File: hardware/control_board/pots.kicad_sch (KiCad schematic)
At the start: 38 parts, among them IC4 4051, IC5 4051, IC6 4051, IC7 4051

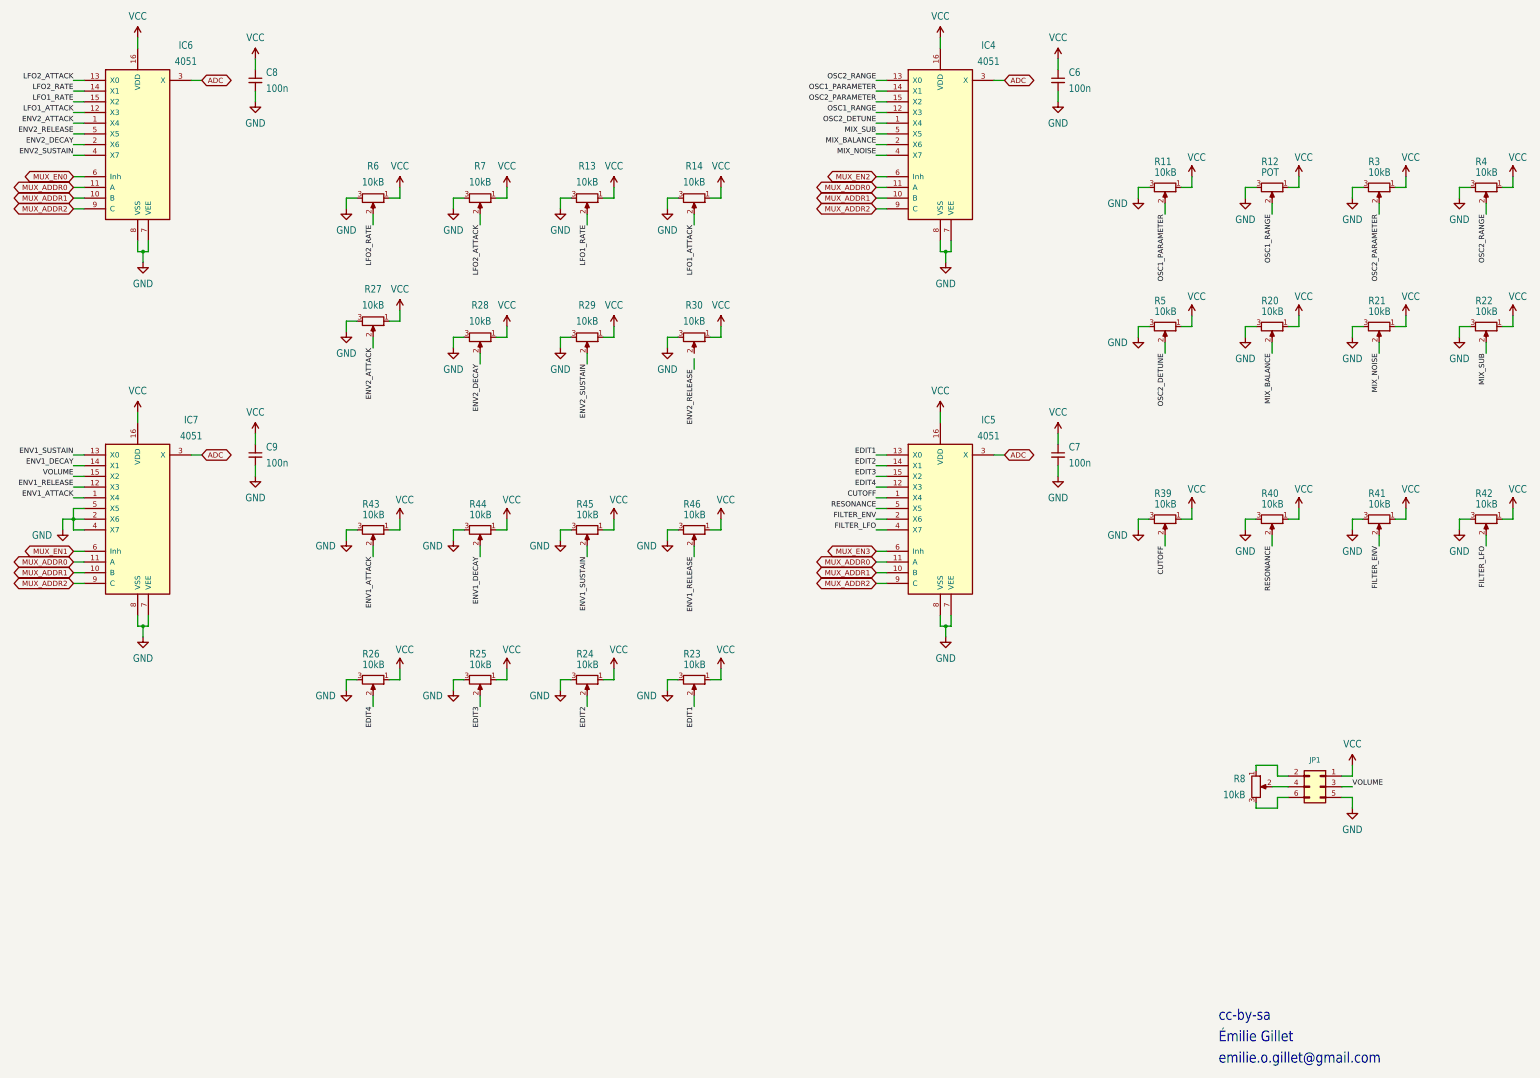
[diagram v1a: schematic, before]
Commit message: move all logic components to daughterboard, move MIDI to new board
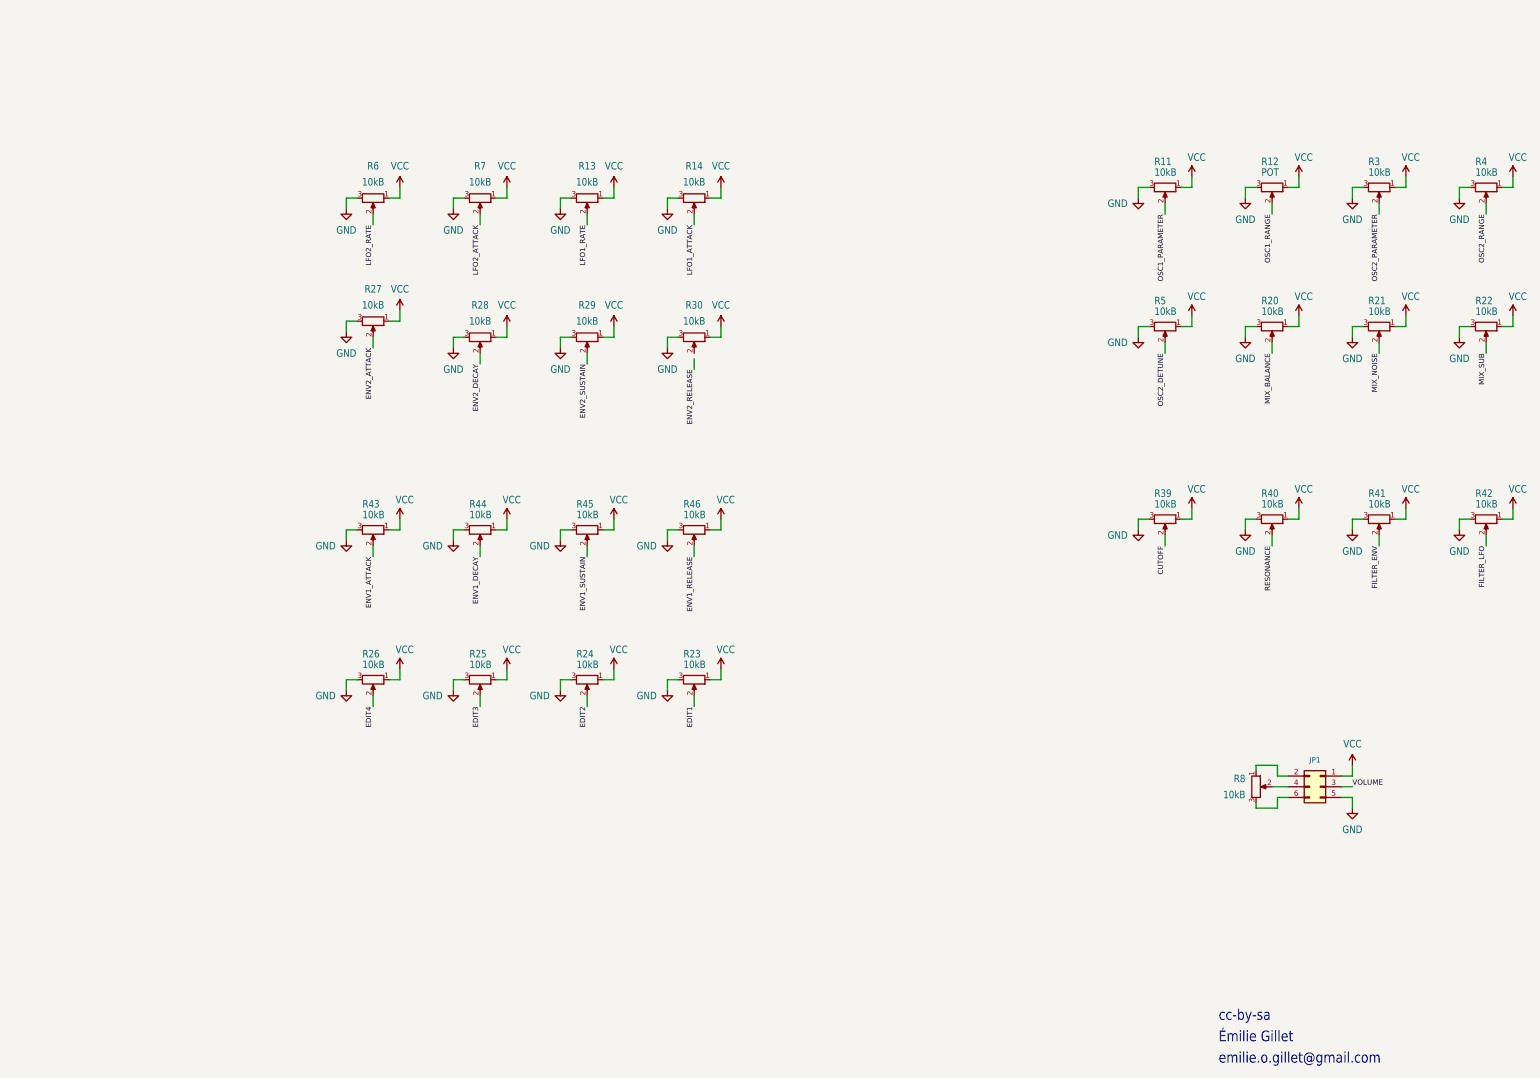
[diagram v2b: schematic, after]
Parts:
- removed C6, C7, C8, C9: 100n, shruthi_control_board_xt_v03:C025-024X044, symbol Device:C_Small
- removed IC4, IC5, IC6, IC7: 4051, Package_DIP:DIP-16_W7.62mm_Socket_LongPads, symbol 4xxx:4051
